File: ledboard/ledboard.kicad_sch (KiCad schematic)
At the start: 46 parts, among them J1 Barrel_Jack_Switch, J3 Conn_01x02, U1 TPS54332DDA, U2 TPS7A5301BRPSR, U3 TPS2121

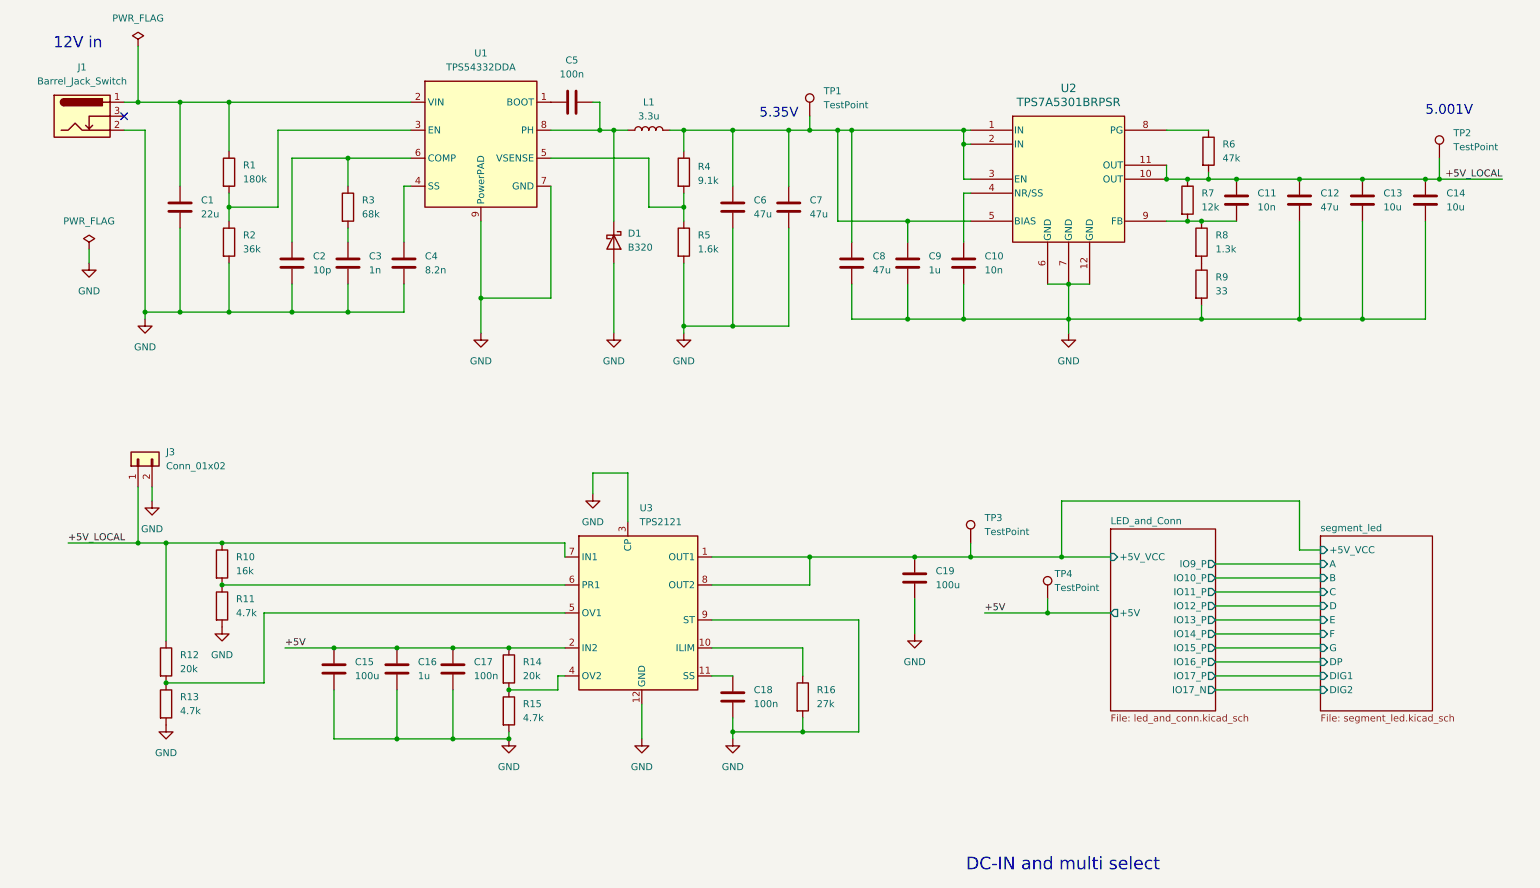
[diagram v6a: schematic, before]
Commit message: LSCS品番を追加. コンデンサの品番を変更します.
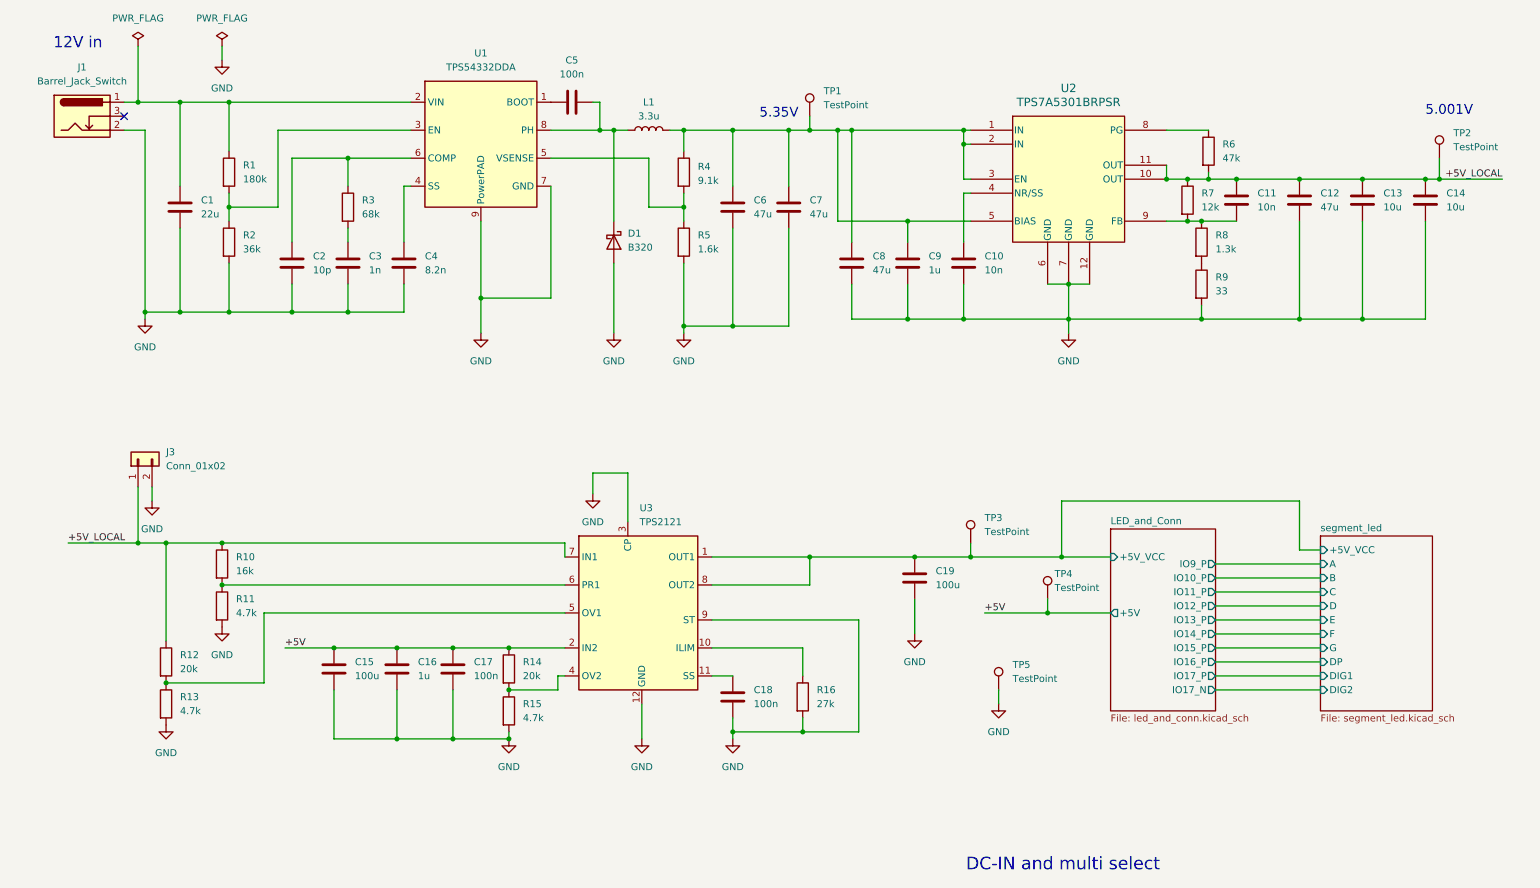
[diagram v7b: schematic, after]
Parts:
- added TP5: TestPoint, TestPoint:TestPoint_Keystone_5000-5004_Miniature, symbol Connector:TestPoint
- C1: LCSC Part # (none) -> C5272872
- C10: LCSC Part # (none) -> C85735
- C11: footprint Capacitor_SMD:C_01005_0402Metric -> Capacitor_SMD:C_0402_1005Metric; LCSC Part # (none) -> C85735; MPN GRM022R61C103ME01 -> GRM155R71C103KA01D
- C12, C6, C7, C8: LCSC Part # (none) -> C385047
- C13, C14: LCSC Part # (none) -> C182375; MPN GRM188R61C106MA73 -> GRM188C81C106MA73D
- C15, C19: LCSC Part # (none) -> C84455
- C16: LCSC Part # (none) -> C162161; MPN GRM155C71A105KE11 -> GRM155C81A105KA12D
- C17, C18: LCSC Part # (none) -> C412246; MPN GRM033C81A104ME14 -> GRM033C81E104ME14
- C2: LCSC Part # (none) -> C161512
- C3: LCSC Part # (none) -> C76942
- C4: LCSC Part # (none) -> C710826; MPN GRM033B11A822JA01 -> GRM033R61E822KA12D
- C5: LCSC Part # (none) -> C412246
- C9: LCSC Part # (none) -> C162161; MPN GRM155B31C105KA12 -> GRM155C81A105KA12D
- D1: LCSC Part # (none) -> C134448
- J1: LCSC Part # (none) -> C3095117
- L1: LCSC Part # (none) -> C1870691
- R1: LCSC Part # (none) -> C123419
- R10: LCSC Part # (none) -> C137788
- R11, R13, R15: LCSC Part # (none) -> C99782
- R12, R14: LCSC Part # (none) -> C105575
- R16: LCSC Part # (none) -> C114614
- R2: LCSC Part # (none) -> C114619
- R3: LCSC Part # (none) -> C114633
- R4: LCSC Part # (none) -> C114639
- R5: LCSC Part # (none) -> C165489
- R6: LCSC Part # (none) -> C105579
- R7: LCSC Part # (none) -> C114659
- R8: LCSC Part # (none) -> C125319
- R9: LCSC Part # (none) -> C108661
- TP1, TP2, TP3, TP4: LCSC Part # (none) -> C238123
- U1: LCSC Part # (none) -> C41312; MPN TPS54332DDA -> TPS54332DDAR
- U2: LCSC Part # (none) -> C2868223
- U3: LCSC Part # (none) -> C485916; MPN TPS2121 -> TPS2121RUXR
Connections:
- net GND: now also TP5.1

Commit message: L1をBOURNS SR8040-3R3Yに変更しました.
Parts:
- J1: now left out of the parts list
- L1: footprint MyLib:SPM7054VC-3R3M-D -> MyLib:IND_BOURNS_SRN8040; LCSC Part # C1870691 -> C780188; MPN SPM7054VC-3R3M-D -> SRN8040-3R3Y; Manufacturer TDK -> BOURNS
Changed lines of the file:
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@@
 		(unit 1)
 		(exclude_from_sim no)
-		(in_bom yes)
+		(in_bom no)
 		(on_board yes)
 		(dnp no)
@@
 			)
 		)
-		(property "Footprint" "MyLib:SPM7054VC-3R3M-D"
+		(property "Footprint" "MyLib:IND_BOURNS_SRN8040"
 			(at 127 39.37 0)
 			(effects
@@
 			)
 		)
-		(property "Datasheet" "~"
+		(property "Datasheet" "https://www.bourns.com/docs/product-datasheets/srn8040.pdf"
 			(at 127 39.37 0)
 			(effects
@@
 			)
 		)
-		(property "Manufacturer" "TDK"
+		(property "Manufacturer" "BOURNS"
 			(at 127 39.37 90)
 			(effects
@@
 			)
 		)
-		(property "MPN" "SPM7054VC-3R3M-D"
+		(property "MPN" "SRN8040-3R3Y"
 			(at 127 39.37 90)
 			(effects
@@
 			)
 		)
-		(property "LCSC Part #" "C1870691"
+		(property "LCSC Part #" "C780188"
 			(at 127 39.37 90)
 			(effects
